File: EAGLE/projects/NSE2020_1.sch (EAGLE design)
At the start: 48 parts, among them CN1 MICROSD, IC1 ADP3338-3.3, X1 MINI-USB-UX60A-MB-5ST

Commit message: 第2次試作で見つかったミスの修正
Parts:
- LED1, LED2, LED3, LED4: device led:LEDSMT1206 -> led:LEDSML0805
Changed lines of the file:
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@@
 <part name="R12" library="rcl" library_urn="urn:adsk.eagle:library:334" deviceset="R-EU_" device="M2012" package3d_urn="urn:adsk.eagle:package:23561/2" value="1k"/>
 <part name="R13" library="rcl" library_urn="urn:adsk.eagle:library:334" deviceset="R-EU_" device="M2012" package3d_urn="urn:adsk.eagle:package:23561/2" value="1k"/>
-<part name="LED1" library="led" library_urn="urn:adsk.eagle:library:259" deviceset="LED" device="SMT1206" package3d_urn="urn:adsk.eagle:package:15796/2"/>
-<part name="LED2" library="led" library_urn="urn:adsk.eagle:library:259" deviceset="LED" device="SMT1206" package3d_urn="urn:adsk.eagle:package:15796/2"/>
-<part name="LED3" library="led" library_urn="urn:adsk.eagle:library:259" deviceset="LED" device="SMT1206" package3d_urn="urn:adsk.eagle:package:15796/2"/>
+<part name="LED1" library="led" library_urn="urn:adsk.eagle:library:259" deviceset="LED" device="SML0805" package3d_urn="urn:adsk.eagle:package:15830/1"/>
+<part name="LED2" library="led" library_urn="urn:adsk.eagle:library:259" deviceset="LED" device="SML0805" package3d_urn="urn:adsk.eagle:package:15830/1"/>
+<part name="LED3" library="led" library_urn="urn:adsk.eagle:library:259" deviceset="LED" device="SML0805" package3d_urn="urn:adsk.eagle:package:15830/1"/>
 <part name="GND11" library="supply1" library_urn="urn:adsk.eagle:library:371" deviceset="GND" device=""/>
 <part name="BUS1" library="databus" deviceset="DATABUS" device=""/>
@@
 <part name="SWD" library="pinhead" library_urn="urn:adsk.eagle:library:325" deviceset="PINHD-1X3" device="" package3d_urn="urn:adsk.eagle:package:22458/2"/>
 <part name="GND16" library="supply1" library_urn="urn:adsk.eagle:library:371" deviceset="GND" device=""/>
-<part name="LED4" library="led" library_urn="urn:adsk.eagle:library:259" deviceset="LED" device="SMT1206" package3d_urn="urn:adsk.eagle:package:15796/2"/>
+<part name="LED4" library="led" library_urn="urn:adsk.eagle:library:259" deviceset="LED" device="SML0805" package3d_urn="urn:adsk.eagle:package:15830/1"/>
 <part name="R14" library="rcl" library_urn="urn:adsk.eagle:library:334" deviceset="R-EU_" device="M2012" package3d_urn="urn:adsk.eagle:package:23561/2" value="1k"/>
 <part name="GND17" library="supply1" library_urn="urn:adsk.eagle:library:371" deviceset="GND" device=""/>

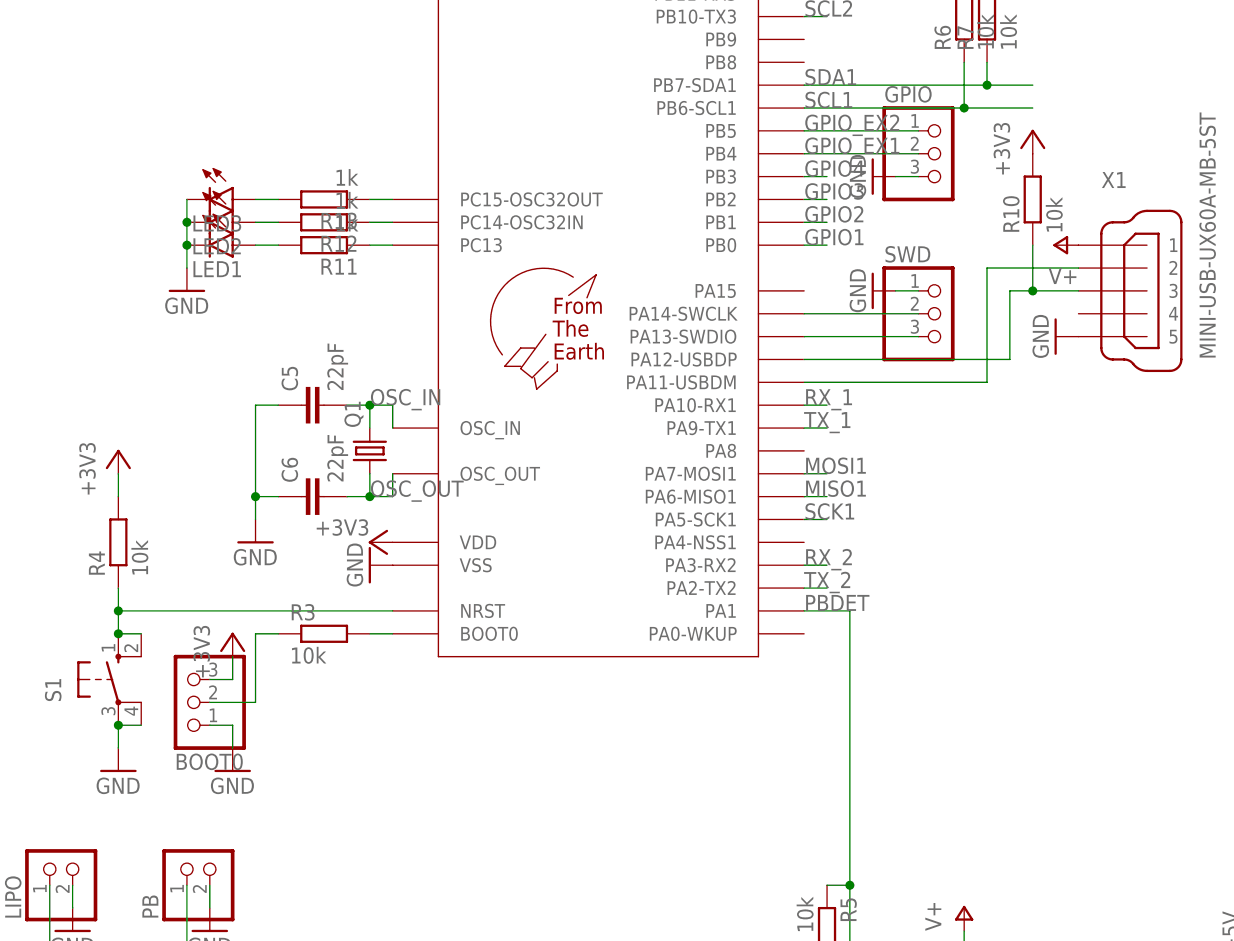
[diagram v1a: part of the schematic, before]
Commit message: 第3次試作修正(USB抵抗、BOOT1プルダウン)
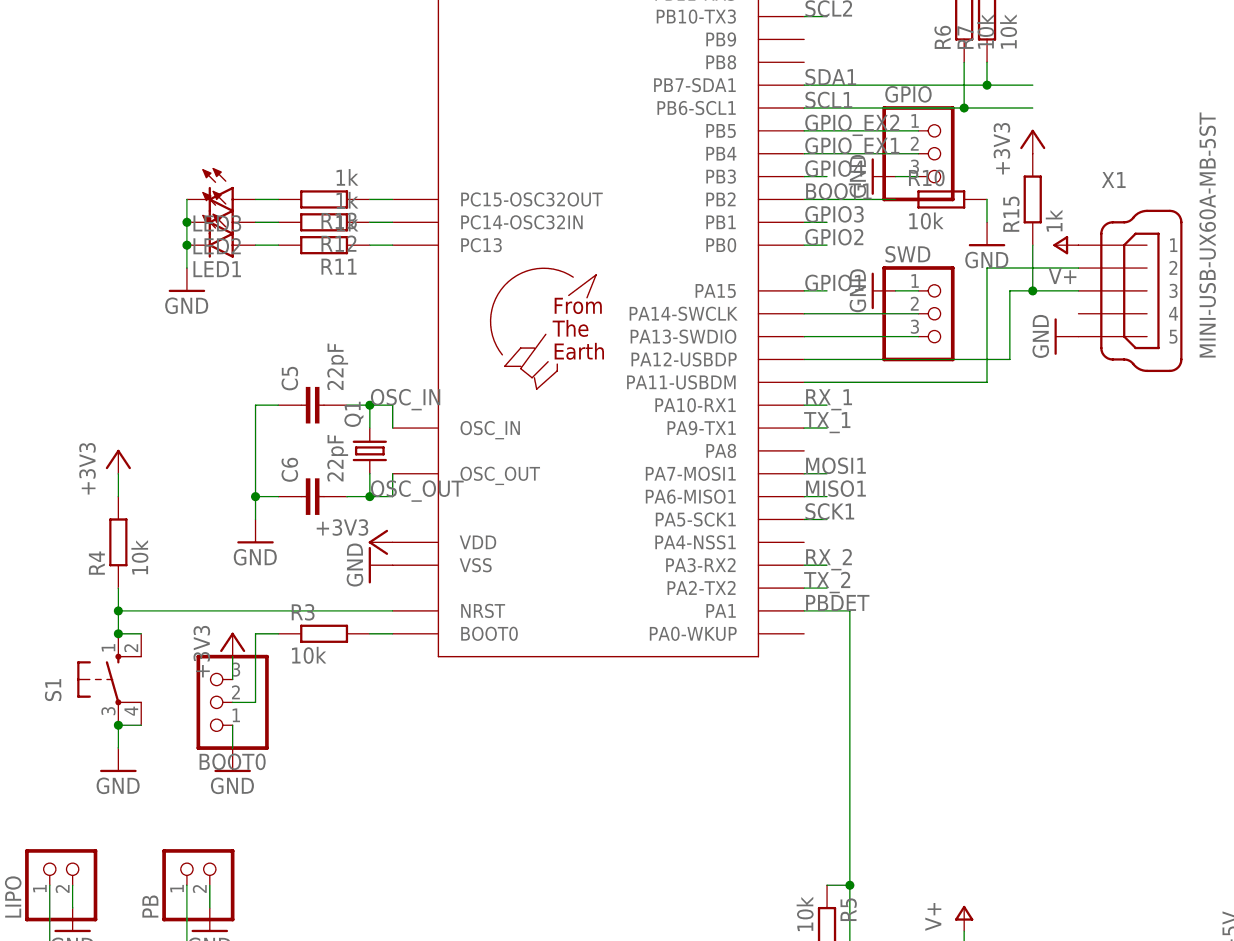
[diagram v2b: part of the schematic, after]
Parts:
- added R15: 1k, rcl:R-EU_M2012
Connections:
- new net BOOT1: MCU1.PB2, R10.1
- net +3V3: now also R15.2; no longer R10.2
- net DP: now also R15.1; no longer R10.1
- net GND: now also R10.2
- net GPIO1: now also MCU1.PA15; no longer MCU1.PB0
- net GPIO2: now also MCU1.PB0; no longer MCU1.PB1
- net GPIO3: now also MCU1.PB1; no longer MCU1.PB2
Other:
- moved on the sheet: BOOT0, R10
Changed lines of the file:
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@@
 <part name="GND6" library="supply1" library_urn="urn:adsk.eagle:library:371" deviceset="GND" device=""/>
 <part name="MCU1" library="STM32F103C8T6" deviceset="STM32F103C8T6" device=""/>
-<part name="BOOT0" library="pinhead" library_urn="urn:adsk.eagle:library:325" deviceset="PINHD-1X3" device="" package3d_urn="urn:adsk.eagle:package:22458/2"/>
 <part name="R3" library="rcl" library_urn="urn:adsk.eagle:library:334" deviceset="R-EU_" device="M2012" package3d_urn="urn:adsk.eagle:package:23561/2" value="10k"/>
 <part name="+3V3" library="supply1" library_urn="urn:adsk.eagle:library:371" deviceset="+3V3" device=""/>
@@
 <part name="FET4" library="2SJ681" deviceset="2SJ681" device=""/>
 <part name="FET3" library="2SJ681" deviceset="2SJ681" device=""/>
-<part name="R10" library="rcl" library_urn="urn:adsk.eagle:library:334" deviceset="R-EU_" device="M2012" package3d_urn="urn:adsk.eagle:package:23561/2" value="10k"/>
+<part name="R15" library="rcl" library_urn="urn:adsk.eagle:library:334" deviceset="R-EU_" device="M2012" package3d_urn="urn:adsk.eagle:package:23561/2" value="1k"/>
 <part name="R9" library="rcl" library_urn="urn:adsk.eagle:library:334" deviceset="R-EU_" device="M2012" package3d_urn="urn:adsk.eagle:package:23561/2" value="10k"/>
 <part name="+3V11" library="supply1" library_urn="urn:adsk.eagle:library:371" deviceset="+3V3" device=""/>
 <part name="+3V12" library="supply1" library_urn="urn:adsk.eagle:library:371" deviceset="+3V3" device=""/>
 <part name="U$1" library="logo" deviceset="F.T.E.LOGO" device=""/>
+<part name="R10" library="rcl" library_urn="urn:adsk.eagle:library:334" deviceset="R-EU_" device="M2012" package3d_urn="urn:adsk.eagle:package:23561/2" value="10k"/>
+<part name="GND18" library="supply1" library_urn="urn:adsk.eagle:library:371" deviceset="GND" device=""/>
+<part name="BOOT0" library="pinhead" library_urn="urn:adsk.eagle:library:325" deviceset="PINHD-1X3" device="" package3d_urn="urn:adsk.eagle:package:22458/2"/>
 </parts>
 <sheets>
@@
 <attribute name="VALUE" x="25.4" y="152.4" size="1.778" layer="96"/>
 </instance>
-<instance part="BOOT0" gate="A" x="-5.08" y="66.04" smashed="yes" rot="R180">
-<attribute name="NAME" x="1.27" y="60.325" size="1.778" layer="95" rot="R180"/>
-<attribute name="VALUE" x="1.27" y="73.66" size="1.778" layer="96" rot="R180"/>
-</instance>
 <instance part="R3" gate="G$1" x="10.16" y="73.66" smashed="yes">
 <attribute name="NAME" x="6.35" y="75.1586" size="1.778" layer="95"/>
@@
 <instance part="FET4" gate="G$1" x="96.52" y="12.7" smashed="yes" rot="MR180"/>
 <instance part="FET3" gate="G$1" x="83.82" y="12.7" smashed="yes" rot="R180"/>
-<instance part="R10" gate="G$1" x="88.9" y="121.92" smashed="yes" rot="R90">
+<instance part="R15" gate="G$1" x="88.9" y="121.92" smashed="yes" rot="R90">
 <attribute name="NAME" x="87.4014" y="118.11" size="1.778" layer="95" rot="R90"/>
 <attribute name="VALUE" x="92.202" y="118.11" size="1.778" layer="96" rot="R90"/>
@@
 </instance>
 <instance part="U$1" gate="G$1" x="35.56" y="109.22" smashed="yes"/>
+<instance part="R10" gate="G$1" x="78.74" y="121.92" smashed="yes">
+<attribute name="NAME" x="74.93" y="123.4186" size="1.778" layer="95"/>
+<attribute name="VALUE" x="74.93" y="118.618" size="1.778" layer="96"/>
+</instance>
+<instance part="GND18" gate="1" x="83.82" y="116.84" smashed="yes">
+<attribute name="VALUE" x="81.28" y="114.3" size="1.778" layer="96"/>
+</instance>
+<instance part="BOOT0" gate="A" x="-2.54" y="66.04" smashed="yes" rot="R180">
+<attribute name="NAME" x="3.81" y="60.325" size="1.778" layer="95" rot="R180"/>
+<attribute name="VALUE" x="3.81" y="73.66" size="1.778" layer="96" rot="R180"/>
+</instance>
 </instances>
 <busses>
@@
 </segment>
 <segment>
+<wire x1="0" y1="63.5" x2="0" y2="60.96" width="0.1524" layer="91"/>
+<pinref part="GND7" gate="1" pin="GND"/>
 <pinref part="BOOT0" gate="A" pin="1"/>
-<wire x1="-2.54" y1="63.5" x2="0" y2="63.5" width="0.1524" layer="91"/>
-<pinref part="GND7" gate="1" pin="GND"/>
-<wire x1="0" y1="60.96" x2="0" y2="63.5" width="0.1524" layer="91"/>
 </segment>
 <segment>
@@
 <pinref part="GPIO" gate="A" pin="3"/>
 <wire x1="73.66" y1="124.46" x2="76.2" y2="124.46" width="0.1524" layer="91"/>
+</segment>
+<segment>
+<pinref part="R10" gate="G$1" pin="2"/>
+<pinref part="GND18" gate="1" pin="GND"/>
+<wire x1="83.82" y1="121.92" x2="83.82" y2="119.38" width="0.1524" layer="91"/>
 </segment>
 </net>
@@
 </segment>
 <segment>
-<pinref part="BOOT0" gate="A" pin="3"/>
-<wire x1="-2.54" y1="68.58" x2="0" y2="68.58" width="0.1524" layer="91"/>
 <wire x1="0" y1="68.58" x2="0" y2="71.12" width="0.1524" layer="91"/>
 <pinref part="+3V3" gate="G$1" pin="+3V3"/>
+<pinref part="BOOT0" gate="A" pin="3"/>
 </segment>
 <segment>
@@
 </segment>
 <segment>
-<pinref part="R10" gate="G$1" pin="2"/>
+<pinref part="R15" gate="G$1" pin="2"/>
 <pinref part="+3V11" gate="G$1" pin="+3V3"/>
 </segment>
@@
 <net name="BOOT0" class="1">
 <segment>
-<pinref part="BOOT0" gate="A" pin="2"/>
-<wire x1="2.54" y1="66.04" x2="-2.54" y2="66.04" width="0.1524" layer="91"/>
 <wire x1="2.54" y1="66.04" x2="2.54" y2="73.66" width="0.1524" layer="91"/>
 <pinref part="R3" gate="G$1" pin="1"/>
 <wire x1="2.54" y1="73.66" x2="5.08" y2="73.66" width="0.1524" layer="91"/>
+<pinref part="BOOT0" gate="A" pin="2"/>
+<wire x1="2.54" y1="66.04" x2="0" y2="66.04" width="0.1524" layer="91"/>
 </segment>
 </net>
@@
 </segment>
 <segment>
+<pinref part="MCU1" gate="G$1" pin="PA15"/>
+<wire x1="63.5" y1="111.76" x2="66.04" y2="111.76" width="0.1524" layer="91"/>
+<label x="63.5" y="111.76" size="1.778" layer="95"/>
+</segment>
+</net>
+<net name="GPIO2" class="1">
+<segment>
+<pinref part="BUS1" gate="G$1" pin="GPIO2"/>
+<wire x1="165.1" y1="96.52" x2="162.56" y2="96.52" width="0.1524" layer="91"/>
+<label x="162.56" y="96.52" size="1.778" layer="95"/>
+</segment>
+<segment>
+<pinref part="BUS2" gate="G$1" pin="GPIO2"/>
+<wire x1="165.1" y1="60.96" x2="162.56" y2="60.96" width="0.1524" layer="91"/>
+<label x="162.56" y="60.96" size="1.778" layer="95"/>
+</segment>
+<segment>
 <pinref part="MCU1" gate="G$1" pin="PB0"/>
 <wire x1="66.04" y1="116.84" x2="63.5" y2="116.84" width="0.1524" layer="91"/>
@@
 </segment>
 </net>
-<net name="GPIO2" class="1">
-<segment>
-<pinref part="BUS1" gate="G$1" pin="GPIO2"/>
-<wire x1="165.1" y1="96.52" x2="162.56" y2="96.52" width="0.1524" layer="91"/>
-<label x="162.56" y="96.52" size="1.778" layer="95"/>
-</segment>
-<segment>
-<pinref part="BUS2" gate="G$1" pin="GPIO2"/>
-<wire x1="165.1" y1="60.96" x2="162.56" y2="60.96" width="0.1524" layer="91"/>
-<label x="162.56" y="60.96" size="1.778" layer="95"/>
+<net name="GPIO3" class="1">
+<segment>
+<pinref part="BUS1" gate="G$1" pin="GPIO3"/>
+<wire x1="165.1" y1="93.98" x2="162.56" y2="93.98" width="0.1524" layer="91"/>
+<label x="162.56" y="93.98" size="1.778" layer="95"/>
+</segment>
+<segment>
+<pinref part="BUS2" gate="G$1" pin="GPIO3"/>
+<wire x1="165.1" y1="58.42" x2="162.56" y2="58.42" width="0.1524" layer="91"/>
+<label x="162.56" y="58.42" size="1.778" layer="95"/>
 </segment>
 <segment>
@@
 <wire x1="66.04" y1="119.38" x2="63.5" y2="119.38" width="0.1524" layer="91"/>
 <label x="63.5" y="119.38" size="1.778" layer="95"/>
-</segment>
-</net>
-<net name="GPIO3" class="1">
-<segment>
-<pinref part="BUS1" gate="G$1" pin="GPIO3"/>
-<wire x1="165.1" y1="93.98" x2="162.56" y2="93.98" width="0.1524" layer="91"/>
-<label x="162.56" y="93.98" size="1.778" layer="95"/>
-</segment>
-<segment>
-<pinref part="BUS2" gate="G$1" pin="GPIO3"/>
-<wire x1="165.1" y1="58.42" x2="162.56" y2="58.42" width="0.1524" layer="91"/>
-<label x="162.56" y="58.42" size="1.778" layer="95"/>
-</segment>
-<segment>
-<pinref part="MCU1" gate="G$1" pin="PB2"/>
-<wire x1="66.04" y1="121.92" x2="63.5" y2="121.92" width="0.1524" layer="91"/>
-<label x="63.5" y="121.92" size="1.778" layer="95"/>
 </segment>
 </net>
@@
 <wire x1="88.9" y1="116.84" x2="88.9" y2="111.76" width="0.1524" layer="91"/>
 <junction x="88.9" y="111.76"/>
-<pinref part="R10" gate="G$1" pin="1"/>
+<pinref part="R15" gate="G$1" pin="1"/>
 </segment>
 </net>
@@
 </segment>
 </net>
+<net name="BOOT1" class="1">
+<segment>
+<pinref part="MCU1" gate="G$1" pin="PB2"/>
+<wire x1="63.5" y1="121.92" x2="73.66" y2="121.92" width="0.1524" layer="91"/>
+<pinref part="R10" gate="G$1" pin="1"/>
+<label x="63.5" y="121.92" size="1.778" layer="95"/>
+</segment>
+</net>
